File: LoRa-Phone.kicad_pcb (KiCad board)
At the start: 4 copper layers, 81.6 x 102.5 mm, 206 parts, among them IC1 SKY13373-460LF, IC10 TPS22965NTDSGRQ1, IC2 AD8318ACPZ-REEL7, IC3 AD8318ACPZ-REEL7, IC4 TPS2121RUXT, IC5 MAX17048G+T10, IC6 MAX17048G+T10, IC7 TCA9543ADR, IC8 MAX16150AUT+T, IC9 SN74LVC1G74RSE2, J1 Interface, J2 Joystick, J3 L76K, J4 JST_MAIN, J5 Board_1, J6 Board_1, M1 Motor_DC, Q1 AO3400A, Q2 AO3400A, Q3 AO3400A, Q4 AO3401A, SW1 POWER, U1 ESP32-S3-WROOM-2, U10 DRV2605LDGS, U12 RV-3028-C7, U13 SA818S, U14 INA219BxDCN, U15 INA219BxDCN, U16 INA219BxDCN, U17 MCP4725xxx-xCH, U18 TLV3501AIDBV, U19 RIC11-31S10K2-GSMT, U2 TCD-10-23BDX+, U21 WM8960, U23 E22-900M30S, U24 E22-170M30S, U3 MCP23017x-x-ML, U4 BMP390, U5 IS31FL3218-QF, U6 LSM6DSOXTR, U7 BQ24075RGT, U8 MCP23017x-x-ML, U9 BQ24075RGT

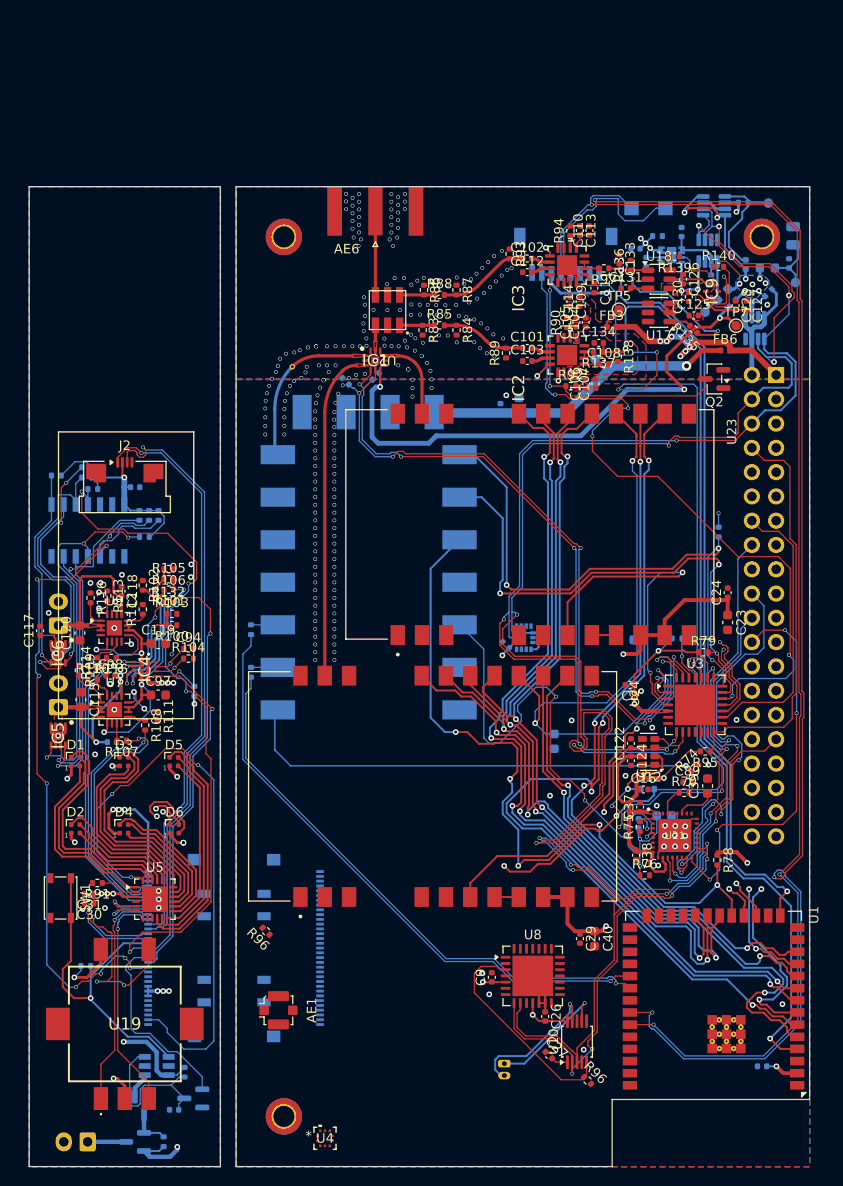
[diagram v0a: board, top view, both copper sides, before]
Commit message: Finishing routing unrouted nets and verifying DRC
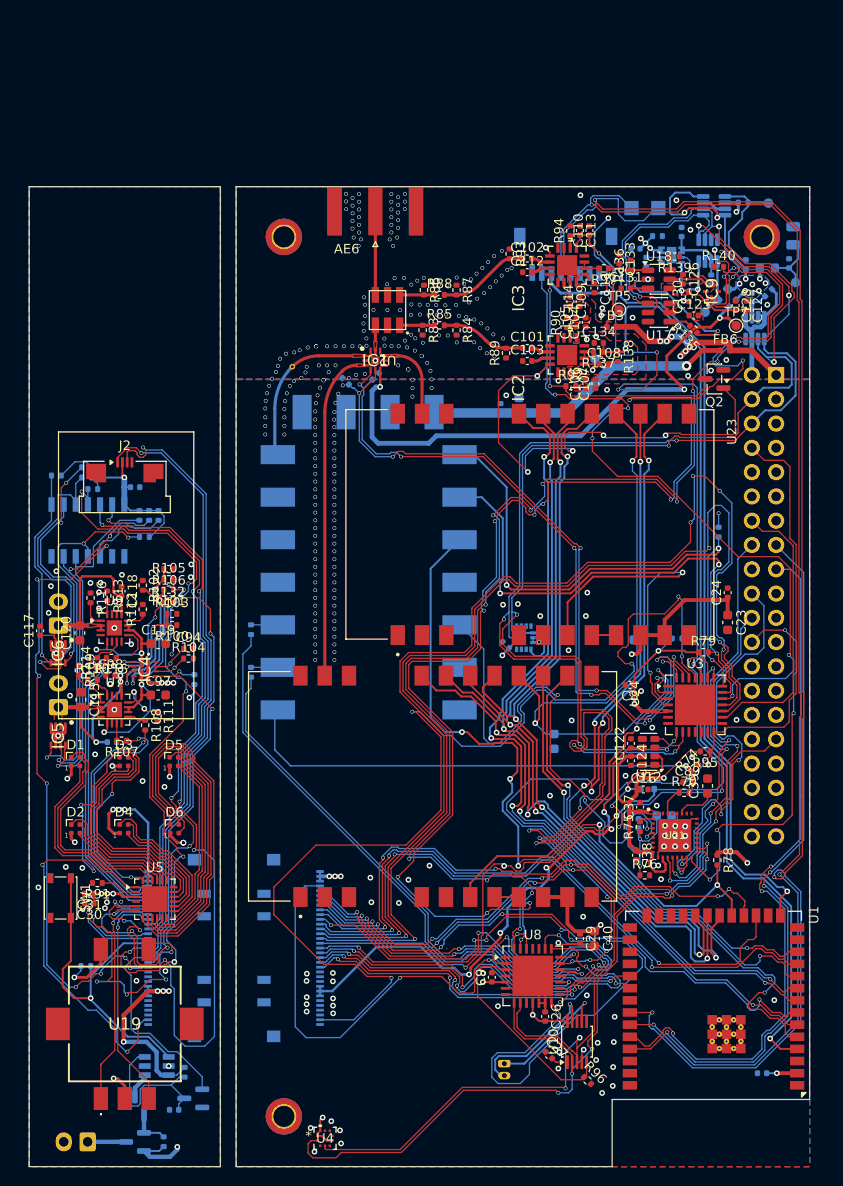
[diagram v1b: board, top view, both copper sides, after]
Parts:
- removed AE1: GNSS, Connector_Coaxial:U.FL_Molex_MCRF_73412-0110_Vertical
- removed the R96 at (119.7, 129.1)
- moved R134 1.22 mm to (112.2, 102.8)
- moved TP1 0.74 mm to (160.8, 53.5)
- moved C4 0.72 mm to (171.6, 144.0)
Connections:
- IC7 pad 12: SCL -> SCL_B
- IC7 pad 13: SDA -> SDA_B
- J5 pad 25: +5V_B -> BAT_OUT
- J5 pad 26: +5V_B -> BAT_OUT
- J5 pad 27: +5V_B -> BAT_OUT
- J6 pad 7: +5V -> BAT_OUT
- J6 pad 8: +5V -> BAT_OUT
- J6 pad 9: +5V -> BAT_OUT
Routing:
- net RF_FAULT: track 4.46 -> 155.4 mm, vias 1 -> 14
- net RF_FAULT_RESET: track 6.73 -> 142.9 mm, vias 0 -> 14
- net BUTTON1: track 7.65 -> 118.1 mm, vias 1 -> 5
- net SDB_1: track 4.79 -> 113.3 mm, vias 1 -> 5
- net BUTTON0: track 9.65 -> 115.1 mm, vias 1 -> 3
- net SDA_B: track 6.50 -> 101.8 mm, vias 1 -> 8
- net SCL: track 207.6 -> 293.4 mm, vias 13 -> 18
- net SDA: track 202.7 -> 288.0 mm, vias 10 -> 16
- net RESET_MCP: track 42.6 -> 123.2 mm, vias 0 -> 6
- net +3V3_RADIO: track 108.4 -> 30.3 mm
- net S3_RXD0: track 0.00 -> 74.9 mm, vias 0 -> 3
- net S3_TXD0: track 0.00 -> 73.9 mm, vias 0 -> 3
- net SCL_B: track 6.39 -> 79.6 mm, vias 1 -> 7
- net JOYSTICK_X: track 4.21 -> 65.9 mm, vias 1 -> 3
- net +3V3: track 242.3 -> 181.6 mm, vias 36 -> 40
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- added copper zone on In2.Cu, net +3V3_GNSS
- added copper zone on In2.Cu, net +3V3_RADIO
- added copper zone on In2.Cu, net +3V3_RAW
- added copper zone on In2.Cu, net +5V

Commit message: Corrected some short circuit and created an AI Agent in KiCAD
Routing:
- net GND: track 35.4 -> 38.0 mm, vias 330 -> 332
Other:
- board text added: "Bonjour"
